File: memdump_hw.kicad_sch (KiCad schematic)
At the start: 46 parts, among them J1 USB_C_Receptacle_USB2.0, J2 SWD, Q1 Q_NMOS_DGS, SW1 RESET, SW2 I2C_A1, SW3 I2C_A2, SW4 I2C_A0, U1 AMS1117-3.3, U2 STM32F103C8Tx, U3 CD4016B, U4 CD4016B, U5 CD4016B, U6 SST39SF040, U7 W25Q128JVS, U8 24LC1025, Y1 12M

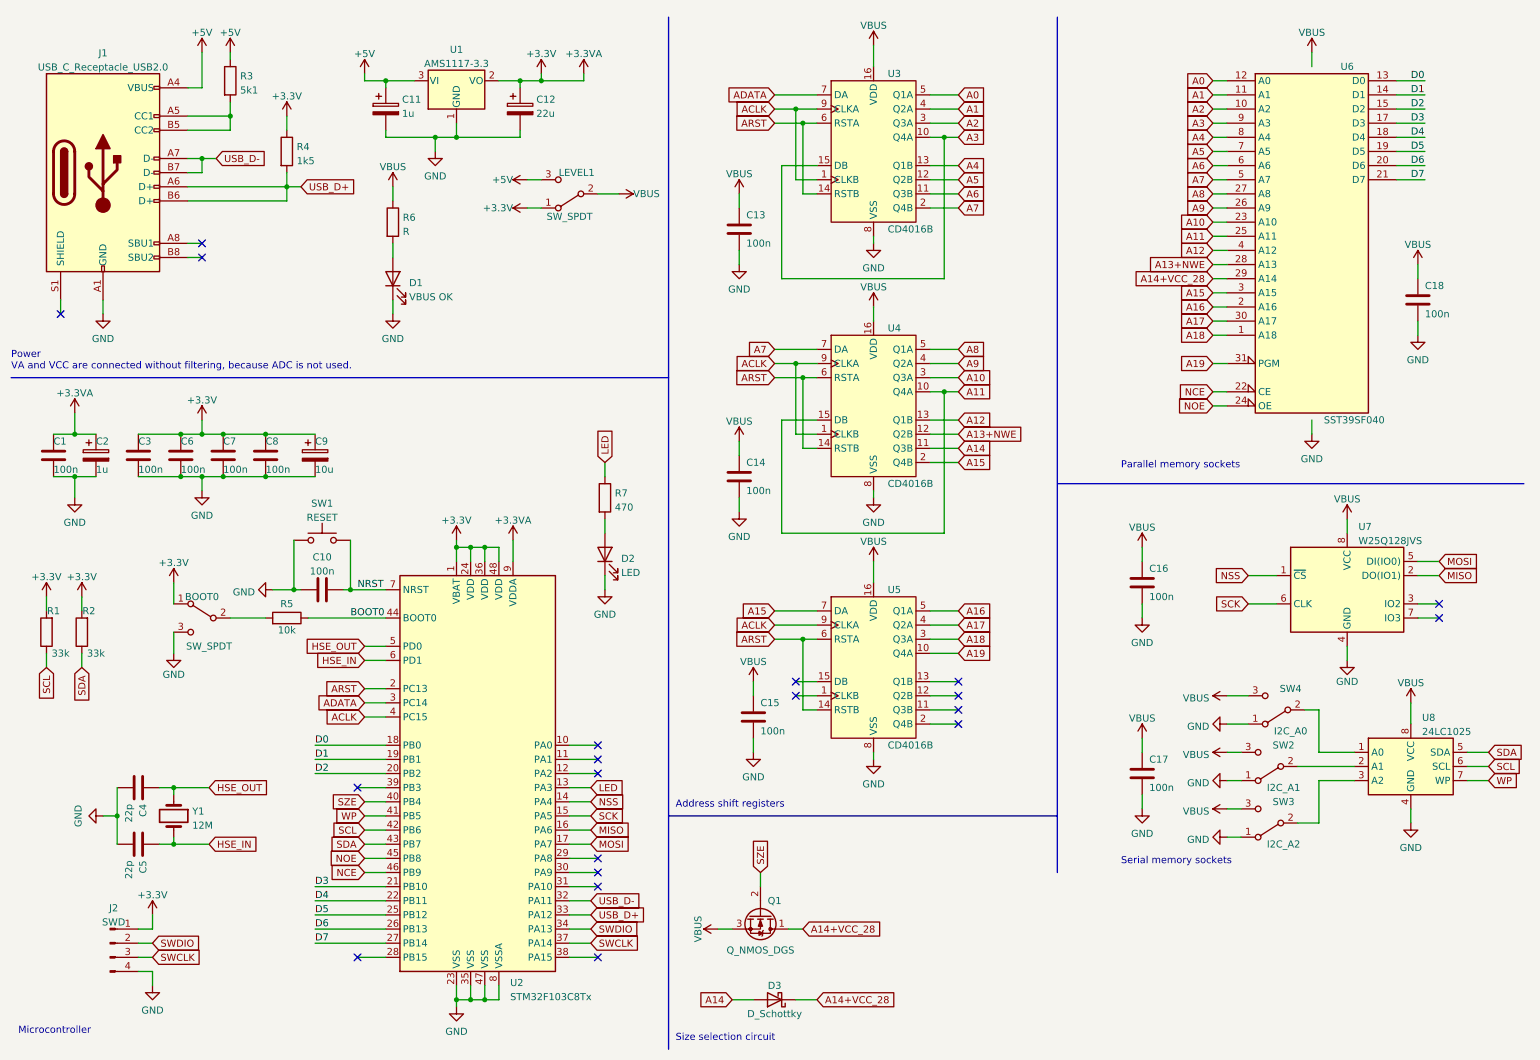
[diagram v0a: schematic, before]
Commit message: *feat: current limiting resistors for protection on all memory pins *feat: begin footprint assignment *feat: I2C address manipulation via the end of the shift register line
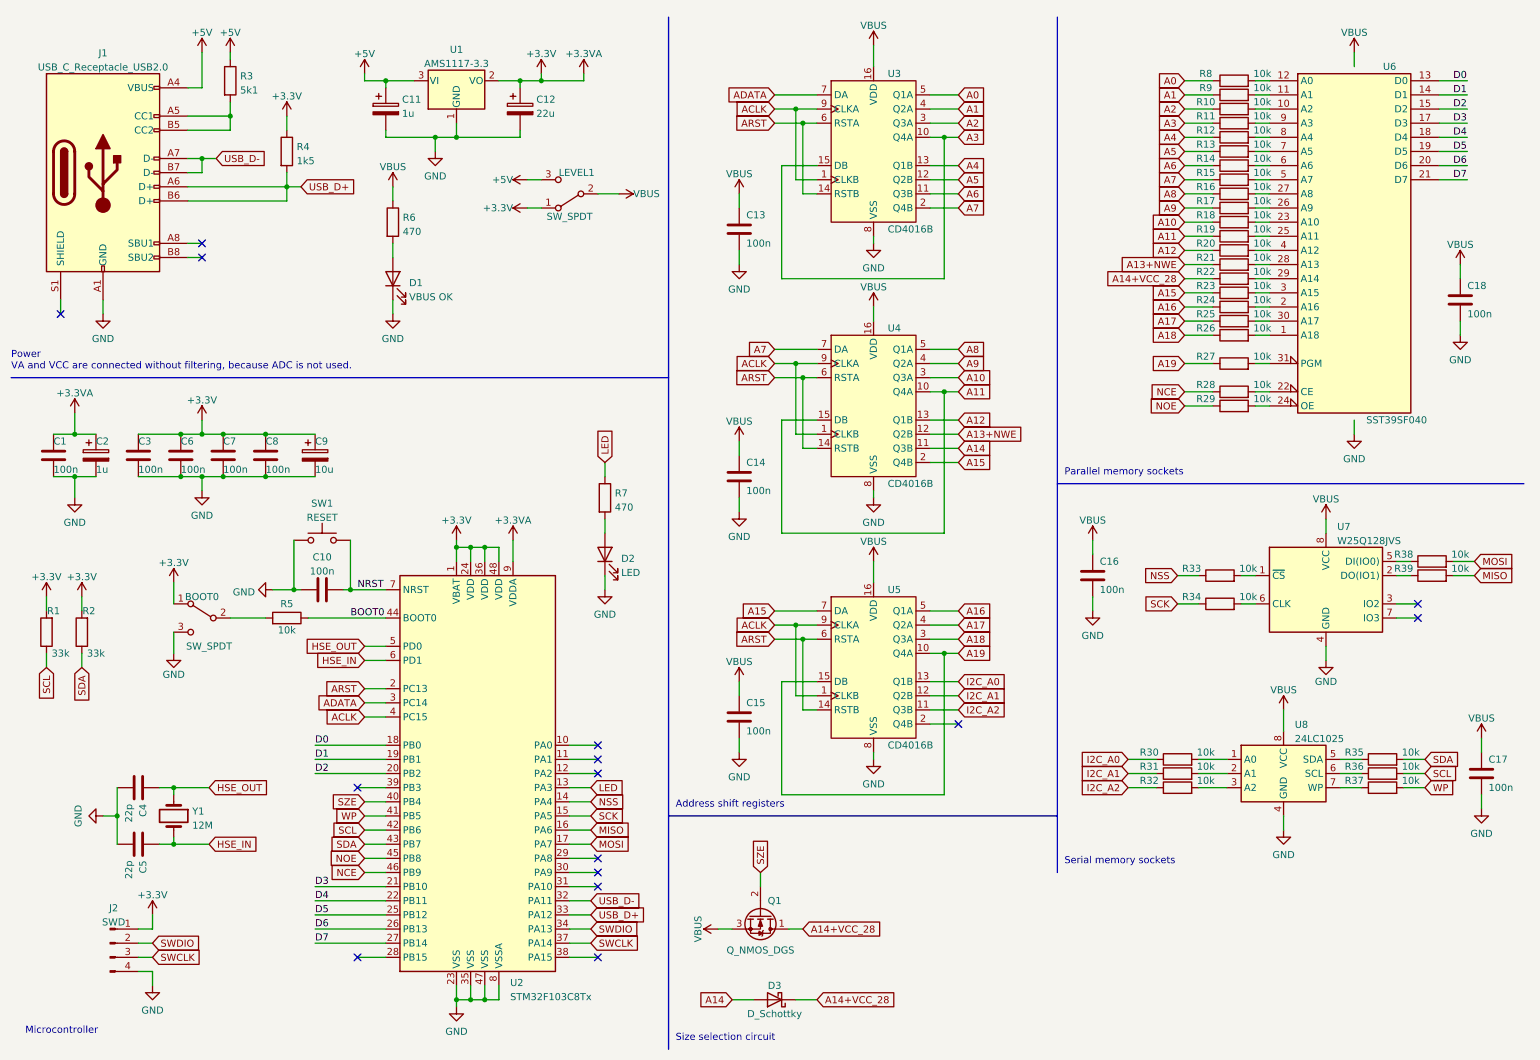
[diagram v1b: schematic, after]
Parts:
- removed SW2: I2C_A1, symbol Switch:SW_SPDT
- removed SW3: I2C_A2, symbol Switch:SW_SPDT
- removed SW4: I2C_A0, symbol Switch:SW_SPDT
- added R10, R11, R12, R13, R14, R15, R16, R17, R18, R19, R20, R21, R22, R23, R24, R25, R26, R27, R28, R29, R30, R31, R32, R33, R34, R35, R36, R37, R38, R39, R8, R9: 10k, Resistor_SMD:R_0805_2012Metric_Pad1.20x1.40mm_HandSolder, symbol Device:R
- C1, C10, C13, C14, C15, C16, C17, C18, C3, C4, C5, C6, C7, C8: footprint (none) -> Capacitor_SMD:C_0805_2012Metric_Pad1.18x1.45mm_HandSolder
- D1, D2: footprint (none) -> LED_SMD:LED_0805_2012Metric_Pad1.15x1.40mm_HandSolder
- J2: footprint (none) -> Connector_PinHeader_2.54mm:PinHeader_1x04_P2.54mm_Horizontal
- R1, R2, R3, R4, R5, R7: footprint (none) -> Resistor_SMD:R_0805_2012Metric_Pad1.20x1.40mm_HandSolder
- R6: value R -> 470; footprint (none) -> Resistor_SMD:R_0805_2012Metric_Pad1.20x1.40mm_HandSolder
- U3, U4, U5: footprint (none) -> Package_DIP:DIP-16_W7.62mm_LongPads
- U6: footprint (none) -> Socket:DIP_Socket-32_W11.9_W12.7_W15.24_W17.78_W18.5_3M_232-1285-00-0602J
- U7: footprint Package_SO:SOIC-8_5.23x5.23mm_P1.27mm -> Package_DIP:DIP-8-16_W7.62mm_Socket
- U8: footprint (none) -> Package_DIP:DIP-8-16_W7.62mm_Socket
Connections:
- net A0: now also R8.1; no longer U6.12 (A0)
- net A1: now also R9.1; no longer U6.11 (A1)
- net A10: now also R18.1; no longer U6.23 (A10)
- net A11: now also R19.1; no longer U6.25 (A11)
- net A12: now also R20.1; no longer U6.4 (A12)
- net A13+NWE: now also R21.1; no longer U6.28 (A13)
- net A14+VCC_28: now also R22.1; no longer U6.29 (A14)
- net A15: now also R23.1; no longer U6.3 (A15)
- net A16: now also R24.1; no longer U6.2 (A16)
- net A17: now also R25.1; no longer U6.30 (A17)
- net A18: now also R26.1; no longer U6.1 (A18)
- net A19: now also U5.15 (DB), R27.1; no longer U6.31 (PGM)
- net A2: now also R10.1; no longer U6.10 (A2)
- net A3: now also R11.1; no longer U6.9 (A3)
- net A4: now also R12.1; no longer U6.8 (A4)
- net A5: now also R13.1; no longer U6.7 (A5)
- net A6: now also R14.1; no longer U6.6 (A6)
- net A7: now also R15.1; no longer U6.5 (A7)
- net A8: now also R16.1; no longer U6.27 (A8)
- net A9: now also R17.1; no longer U6.26 (A9)
- net ACLK: now also U5.1 (CLKB)
- net MISO: now also R39.2; no longer U7.2 (DO(IO1))
- net MOSI: now also R38.2; no longer U7.5 (DI(IO0))
- net NCE: now also R28.1; no longer U6.22 (CE)
- net NOE: now also R29.1; no longer U6.24 (OE)
- net NSS: now also R33.1; no longer U7.1 (~{CS})
- net SCK: now also R34.1; no longer U7.6 (CLK)
- net SCL: now also R36.2; no longer U8.6 (SCL)
- net SDA: now also R35.2; no longer U8.5 (SDA)
- net WP: now also R37.2; no longer U8.7 (WP)
- net at U8.1 (A0): now also R30.2
- net at U8.2 (A1): now also R31.2
- net at U8.3 (A2): now also R32.2
- net I2C_A2: now reaches U5.11 (Q3B)
- net I2C_A2: now also R32.1
- net I2C_A1: now reaches U5.12 (Q2B)
- net I2C_A1: now also R31.1
- net I2C_A0: now reaches U5.13 (Q1B)
- net I2C_A0: now also R30.1
- new net: R19.2, U6.25 (A11)
- new net: R20.2, U6.4 (A12)
- new net: R22.2, U6.29 (A14)
- new net: R37.1, U8.7 (WP)
- new net: R39.1, U7.2 (DO(IO1))
- new net: R17.2, U6.26 (A9)
- new net: R25.2, U6.30 (A17)
- new net: R35.1, U8.5 (SDA)
- new net: R36.1, U8.6 (SCL)
- new net: R26.2, U6.1 (A18)
- new net: R33.2, U7.1 (~{CS})
- new net: R15.2, U6.5 (A7)
- new net: R38.1, U7.5 (DI(IO0))
- new net: R10.2, U6.10 (A2)
- new net: R9.2, U6.11 (A1)
- new net: R8.2, U6.12 (A0)
- new net: R24.2, U6.2 (A16)
- new net: R28.2, U6.22 (CE)
- new net: R18.2, U6.23 (A10)
- new net: R29.2, U6.24 (OE)
- new net: R16.2, U6.27 (A8)
- new net: R21.2, U6.28 (A13)
- new net: R23.2, U6.3 (A15)
- new net: R27.2, U6.31 (PGM)
- new net: R14.2, U6.6 (A6)
- new net: R13.2, U6.7 (A5)
- new net: R12.2, U6.8 (A4)
- new net: R11.2, U6.9 (A3)
- new net: R34.2, U7.6 (CLK)
- no-connect marks 20 -> 15
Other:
- moved on the sheet: C15, C16, C17, C18, U6, U7, U8

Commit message: chore: updated gitignore fix: changed to 4094 fix: better layout
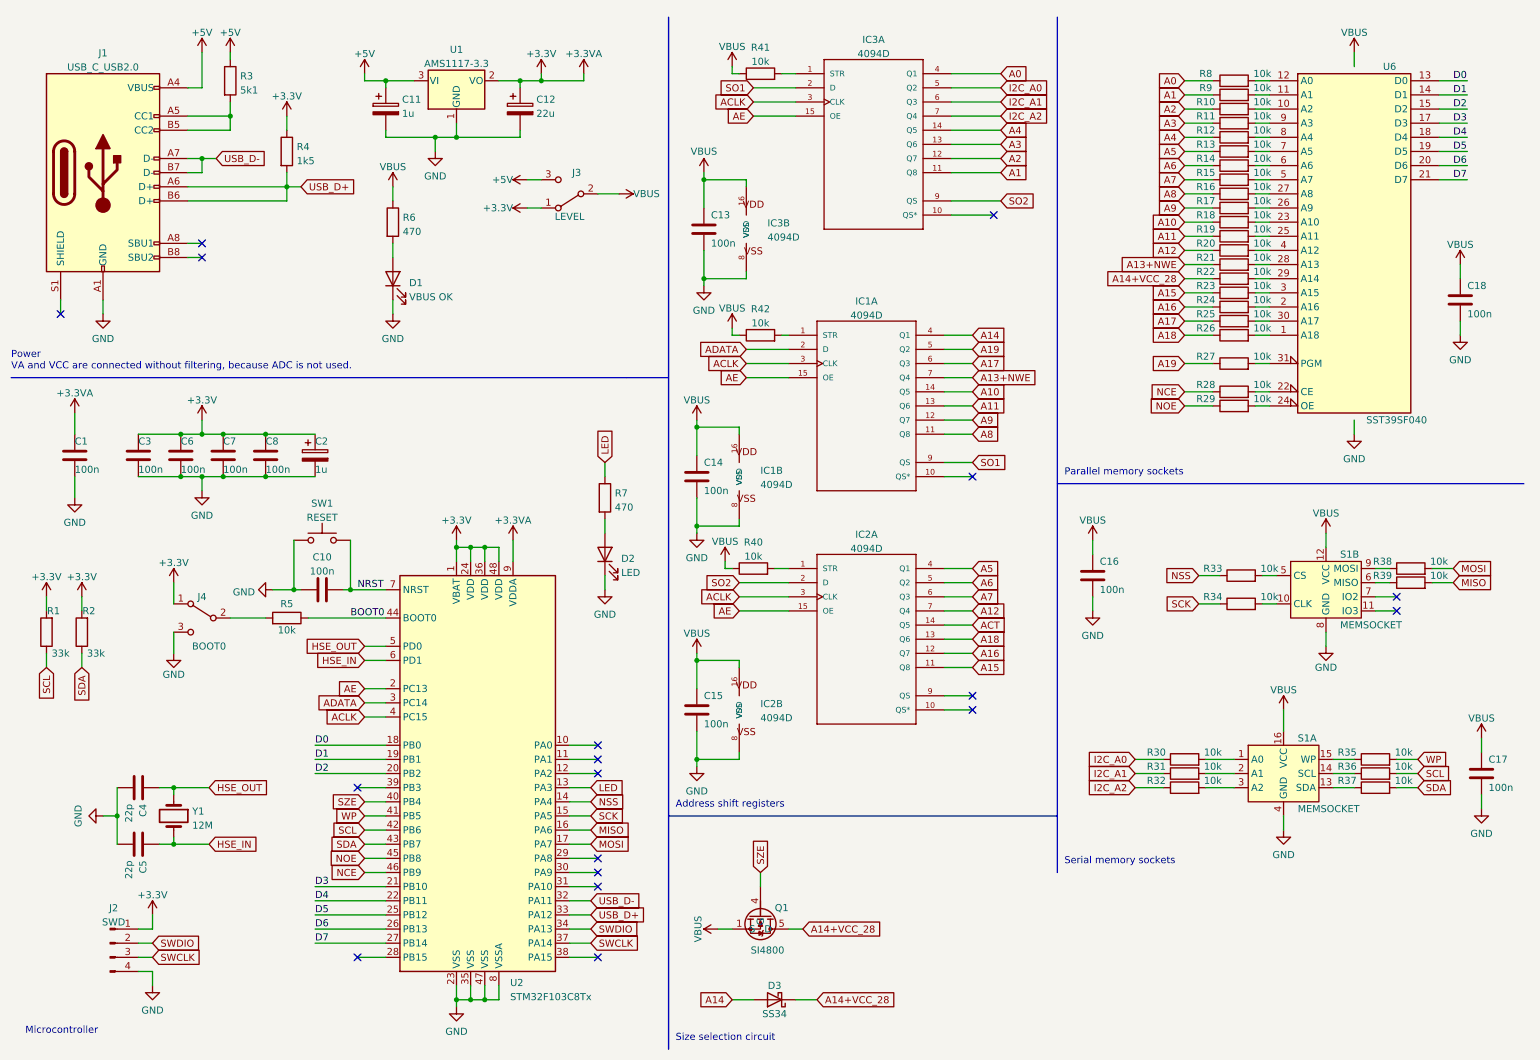
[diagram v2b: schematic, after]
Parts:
- removed C9: 10u, symbol Device:C_Polarized
- removed Q1: Q_NMOS_DGS, symbol Device:Q_NMOS_DGS
- removed U3, U4, U5: CD4016B, Package_DIP:DIP-16_W7.62mm_LongPads, symbol memdump:CD4016B
- removed U7: W25Q128JVS, Package_DIP:DIP-8-16_W7.62mm_Socket, symbol Memory_Flash:W25Q128JVS
- removed U8: 24LC1025, Package_DIP:DIP-8-16_W7.62mm_Socket, symbol Memory_EEPROM:24LC1025
- added IC1, IC2, IC3: 4094D, Package_SO:SOIC-16_3.9x9.9mm_P1.27mm, symbol 40xx:4094D
- added Q1: SI4800, Package_SO:SO-8_3.9x4.9mm_P1.27mm, symbol memdump:SI4800
- added R40, R41, R42: 10k, Resistor_SMD:R_0805_2012Metric_Pad1.20x1.40mm_HandSolder, symbol Device:R
- added S1: MEMSOCKET, Socket:DIP_Socket-16_W4.3_W5.08_W7.62_W10.16_W10.9_3M_216-3340-00-0602J, symbol memdump:MEMSOCKET
- C11, C2: footprint (none) -> Capacitor_SMD:CP_Elec_4x4.5
- C12: footprint (none) -> Capacitor_Tantalum_SMD:CP_EIA-3528-12_Kemet-T_Pad1.50x2.35mm_HandSolder
- D3: value D_Schottky -> SS34; footprint (none) -> Diode_SMD:D_1206_3216Metric_Pad1.42x1.75mm_HandSolder
- J1: value USB_C_Receptacle_USB2.0 -> USB_C_USB2.0; footprint (none) -> Connector_USB:USB_C_Receptacle_HRO_TYPE-C-31-M-12
- J2: footprint Connector_PinHeader_2.54mm:PinHeader_1x04_P2.54mm_Horizontal -> Connector_PinHeader_2.54mm:PinHeader_1x04_P2.54mm_Vertical
- J3: renamed from LEVEL1; value SW_SPDT -> LEVEL; footprint (none) -> Connector_PinHeader_2.54mm:PinHeader_1x03_P2.54mm_Vertical
- J4: renamed from BOOT0; value SW_SPDT -> BOOT0; footprint (none) -> Connector_PinHeader_2.54mm:PinHeader_1x03_P2.54mm_Vertical
- SW1: footprint (none) -> Button_Switch_SMD:SW_Push_SPST_NO_Alps_SKRK
- Y1: footprint (none) -> Crystal:Crystal_HC18-U_Vertical
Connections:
- net A0: now also IC3.4 (Q1)
- net A1: now also IC3.11 (Q8)
- net A10: now also IC1.14 (Q5)
- net A11: now also IC1.13 (Q6)
- net A12: now also IC2.7 (Q4)
- net A13+NWE: now also IC1.7 (Q4)
- net A14: now also IC1.4 (Q1)
- net A14+VCC_28: now also Q1.5 (D), Q1.6 (D), Q1.7 (D), Q1.8 (D)
- net A15: now also IC2.11 (Q8)
- net A16: now also IC2.12 (Q7)
- net A17: now also IC1.6 (Q3)
- net A18: now also IC2.13 (Q6)
- net A19: now also IC1.5 (Q2)
- net A2: now also IC3.12 (Q7)
- net A3: now also IC3.13 (Q6)
- net A4: now also IC3.14 (Q5)
- net A5: now also IC2.4 (Q1)
- net A6: now also IC2.5 (Q2)
- net A7: now also IC2.6 (Q3)
- net A8: now also IC1.11 (Q8)
- net A9: now also IC1.12 (Q7)
- net ACLK: now also IC1.3 (CLK), IC2.3 (CLK), IC3.3 (CLK)
- net ADATA: now also IC1.2 (D)
- net GND: now also IC1.8 (VSS), IC2.8 (VSS), IC3.8 (VSS), S1.4 (GND), S1.8 (GND)
- net I2C_A0: now also IC3.5 (Q2)
- net I2C_A1: now also IC3.6 (Q3)
- net I2C_A2: now also IC3.7 (Q4)
- net SDA: now also R37.2; no longer R35.2
- net SZE: now also Q1.4 (G)
- net VBUS: now also IC1.16 (VDD), IC2.16 (VDD), IC3.16 (VDD), Q1.1 (S), Q1.2 (S), Q1.3 (S), R40.1, R41.1, R42.1, S1.12 (VCC), S1.16 (VCC)
- net WP: now also R35.2; no longer R37.2
- net at R37.1: now also S1.13 (SDA)
- net at R39.1: now also S1.6 (MISO)
- net at R30.2: now also S1.1 (A0)
- net at R31.2: now also S1.2 (A1)
- net at R32.2: now also S1.3 (A2)
- net at R35.1: now also S1.15 (WP)
- net at R36.1: now also S1.14 (SCL)
- net at R33.2: now also S1.5 (CS)
- net at R38.1: now also S1.9 (MOSI)
- net at R34.2: now also S1.10 (CLK)
- net ARST renamed AE
- net AE: now also IC1.15 (OE), IC2.15 (OE), IC3.15 (OE)
- new net: IC3.1 (STR), R41.2
- new net: IC1.1 (STR), R42.2
- new net: IC2.1 (STR), R40.2
- new net ACT: IC2.14 (Q5)
- new net SO1: IC1.9 (QS), IC3.2 (D)
- new net SO2: IC2.2 (D), IC3.9 (QS)
- no-connect marks 15 -> 18
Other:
- moved on the sheet: C1, C13, C14, C15, C2, R30, R31, R32, R33, R34, R35, R36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
